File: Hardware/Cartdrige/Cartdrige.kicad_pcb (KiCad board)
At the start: 2 copper layers, 47.6 x 112.1 mm, 5 parts, among them J1 CARTDRIGE, U1 28C256, U2 28C256

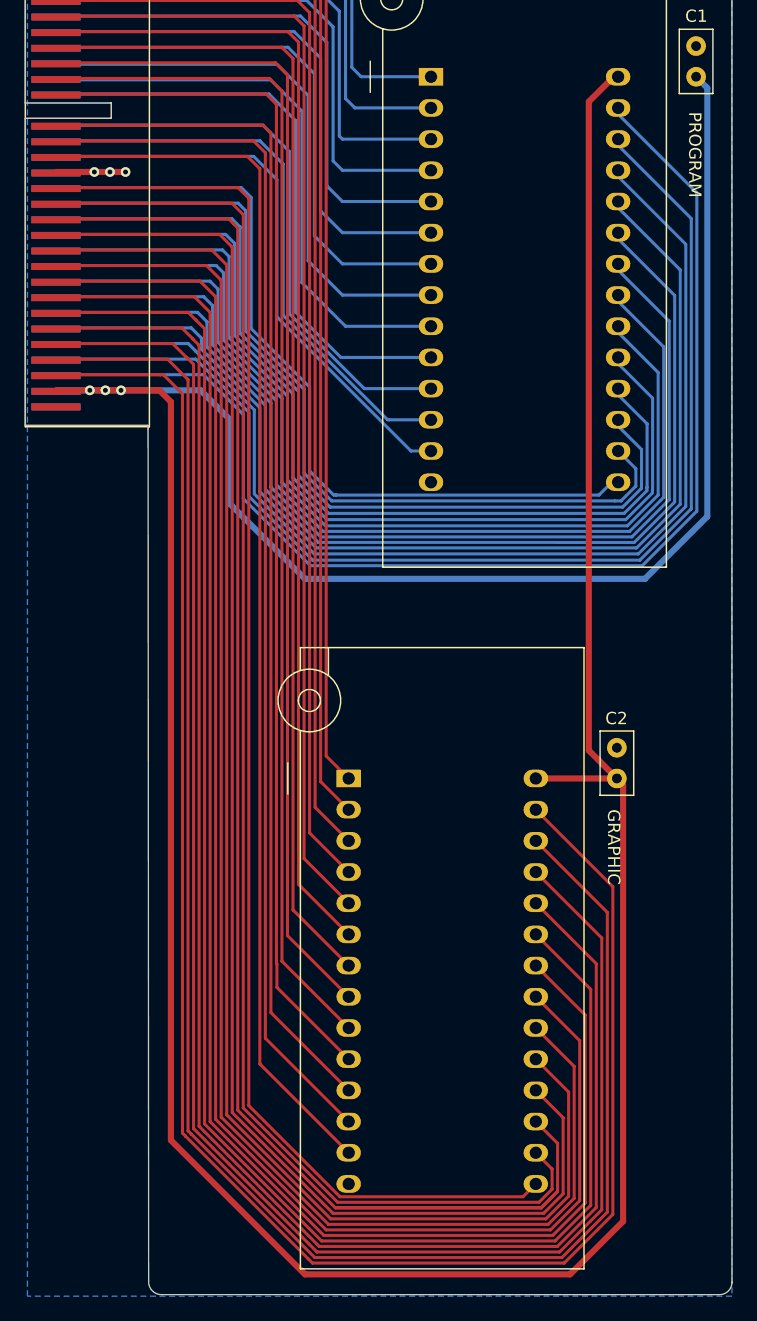
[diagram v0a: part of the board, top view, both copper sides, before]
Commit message: implement graphic loading from ROM
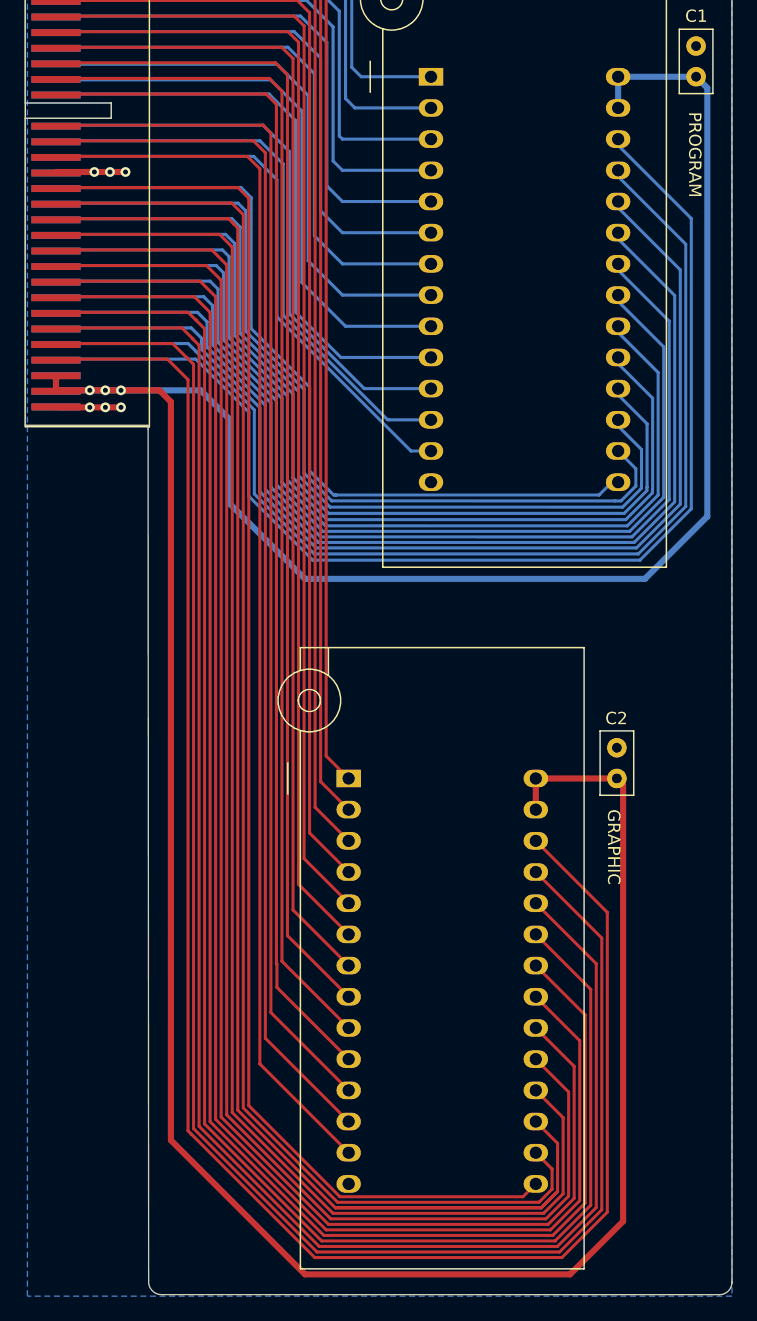
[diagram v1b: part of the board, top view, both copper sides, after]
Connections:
- J1 pad 55: WEA -> +5V
- J1 pad 56: WEB -> +5V
- J1 pad 59: no_connect_57 -> GND
- J1 pad 60: no_connect_58 -> GND
- U1 pad 27: WEA -> +5V
- U2 pad 27: WEB -> +5V
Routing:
- net WEA: track 147.8 -> 0.00 mm
- net WEB: track 100.2 -> 0.00 mm
- net +5V: track 316.5 -> 271.5 mm
- net GND: track 6.27 -> 11.6 mm, vias 3 -> 6

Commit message: Fix
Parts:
- removed C2: 100nF, Capacitor_THT:C_Disc_D5.0mm_W2.5mm_P2.50mm
- removed U2: 28C256, Socket:DIP_Socket-28_W11.9_W12.7_W15.24_W17.78_W18.5_3M_228-1277-00-0602J
- added XiaoNiuNiu: LOGO, Logos:VerySmallCow, F.Cu at (87.9, 32.0)
- J1: value CARTDRIGE -> ROM; footprint Connector_PCBEdge:Samtec_MECF-30-0_-L-DV_2x30_P1.27mm_Polarized_Edge -> Connector_TheRLab:NES_PCBEdge
- U1: footprint Socket:DIP_Socket-28_W11.9_W12.7_W15.24_W17.78_W18.5_3M_228-1277-00-0602J -> Package_DIP:DIP-28_W15.24mm
- moved U1 91.5 mm to (75.9, 34.8), turned to -90 degrees
- moved C1 88.4 mm to (76.1, 53.5), turned to 180 degrees
- moved J1 51.1 mm to (64.4, 64.6), turned to 0 degrees
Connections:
- net /AA14 renamed /A14
- J1 pad 10: /AB5 -> /A0
- J1 pad 11: /AA4 -> /D0
- J1 pad 12: /AB4 -> /D1
- J1 pad 13: /AA3 -> /D2
- J1 pad 14: /AB3 -> GND
- J1 pad 15: /AA2 -> /D3
- J1 pad 16: /AB2 -> /D4
- J1 pad 17: /AA1 -> /D5
- J1 pad 18: /AB1 -> /D6
- J1 pad 19: /AA0 -> /D7
- J1 pad 2: /AB14 -> /A12
- J1 pad 20: /AB0 -> CS
- J1 pad 23: /DA0 -> /A11
- J1 pad 24: /DB0 -> /A9
- J1 pad 25: /DA1 -> /A8
- J1 pad 26: /DB1 -> /A13
- J1 pad 27: /DA2 -> +5V
- J1 pad 28: /DB2 -> +5V
- J1 pad 3: /AA12 -> /A7
- J1 pad 4: /AB12 -> /A6
- J1 pad 5: /AA7 -> /A5
- J1 pad 6: /AB7 -> /A4
- J1 pad 7: /AA6 -> /A3
- J1 pad 8: /AB6 -> /A2
- J1 pad 9: /AA5 -> /A1
- U1 pad 10: /AA0 -> /A0
- U1 pad 11: /DA0 -> /D0
- U1 pad 12: /DA1 -> /D1
- U1 pad 13: /DA2 -> /D2
- U1 pad 15: /DA3 -> /D3
- U1 pad 16: /DA4 -> /D4
- U1 pad 17: /DA5 -> /D5
- U1 pad 18: /DA6 -> /D6
- U1 pad 19: /DA7 -> /D7
- U1 pad 2: /AA12 -> /A12
- U1 pad 20: CSA -> CS
- U1 pad 21: /AA10 -> /A10
- U1 pad 22: OEA -> OE
- U1 pad 23: /AA11 -> /A11
- U1 pad 24: /AA9 -> /A9
- U1 pad 25: /AA8 -> /A8
- U1 pad 26: /AA13 -> /A13
- U1 pad 3: /AA7 -> /A7
- U1 pad 4: /AA6 -> /A6
- U1 pad 5: /AA5 -> /A5
- U1 pad 6: /AA4 -> /A4
- U1 pad 7: /AA3 -> /A3
- U1 pad 8: /AA2 -> /A2
- U1 pad 9: /AA1 -> /A1
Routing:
- net +5V: track 271.5 -> 83.3 mm, vias 3 -> 2
- net /AA13: track 145.2 -> 0.00 mm
- net /AA8: track 142.7 -> 0.00 mm
- net /DA5: track 141.9 -> 0.00 mm
- net /AA9: track 140.4 -> 0.00 mm
- net /AA11: track 137.9 -> 0.00 mm
- net OEA: track 135.5 -> 0.00 mm
- net /AA10: track 133.0 -> 0.00 mm
- net CSA: track 130.5 -> 0.00 mm
- net /DA7: track 128.0 -> 0.00 mm
- net /DA6: track 125.6 -> 0.00 mm
- net /DA4: track 120.7 -> 0.00 mm
- net /DA3: track 116.8 -> 0.00 mm
- net /DA2: track 100.1 -> 0.00 mm
- net /DA1: track 99.2 -> 0.00 mm
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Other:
- board size 47.6 x 112.1 mm -> 80 x 34.3 mm
- board text removed: "GRAPHIC"
- board text removed: "PROGRAM"
